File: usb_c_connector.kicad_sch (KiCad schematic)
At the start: 8 parts, among them J5 USB_C_Receptacle_USB2.0_16P, U4 USBLC6-2SC6

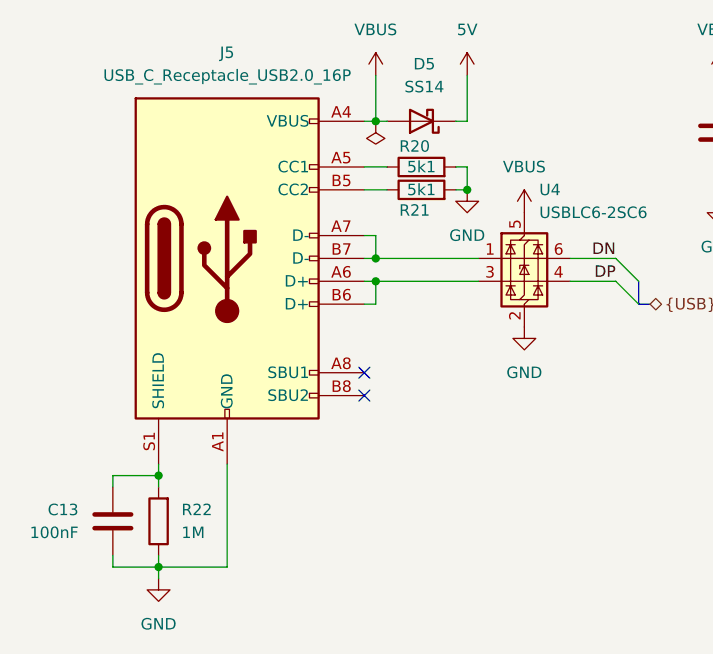
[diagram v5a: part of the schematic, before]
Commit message: Connect remaining tracks
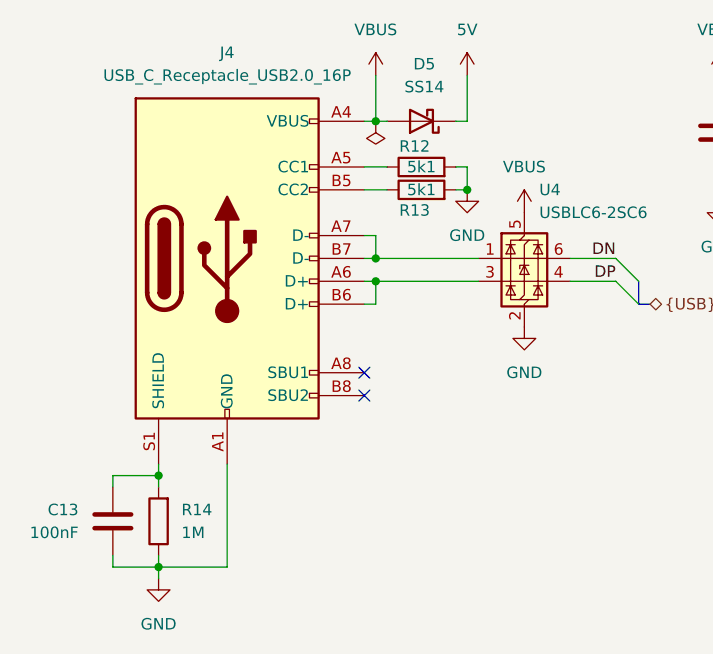
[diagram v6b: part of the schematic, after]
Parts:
- renumbered J5 to J4, R20 to R12, R21 to R13, R22 to R14
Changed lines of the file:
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@@
 		(on_board yes)
 		(dnp no)
-		(property "Reference" "R20"
+		(property "Reference" "R12"
 			(at 142.748 84.074 90)
 			(effects
@@
 			(project "Tumbler2_Redesign"
 				(path "/f3fd8d79-9d35-4c04-811e-2697a2740958/84b20f1f-6e00-4937-92e5-6e005c1bde3e"
-					(reference "R20")
+					(reference "R12")
 					(unit 1)
 				)
@@
 		(on_board yes)
 		(dnp no)
-		(property "Reference" "J5"
+		(property "Reference" "J4"
 			(at 121.92 73.66 0)
 			(effects
@@
 			(project "Tumbler2_Redesign"
 				(path "/f3fd8d79-9d35-4c04-811e-2697a2740958/84b20f1f-6e00-4937-92e5-6e005c1bde3e"
-					(reference "J5")
+					(reference "J4")
 					(unit 1)
 				)
@@
 		(on_board yes)
 		(dnp no)
-		(property "Reference" "R21"
+		(property "Reference" "R13"
 			(at 142.748 91.186 90)
 			(effects
@@
 			(project "Tumbler2_Redesign"
 				(path "/f3fd8d79-9d35-4c04-811e-2697a2740958/84b20f1f-6e00-4937-92e5-6e005c1bde3e"
-					(reference "R21")
+					(reference "R13")
 					(unit 1)
 				)
@@
 		(dnp no)
 		(fields_autoplaced yes)
-		(property "Reference" "R22"
+		(property "Reference" "R14"
 			(at 116.84 124.4599 0)
 			(effects
@@
 			(project "Tumbler2_Redesign"
 				(path "/f3fd8d79-9d35-4c04-811e-2697a2740958/84b20f1f-6e00-4937-92e5-6e005c1bde3e"
-					(reference "R22")
-					(unit 1)
-				)
+					(reference "R14")
+					(unit 1)
+				)

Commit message: cleanup schemati, replaced some caps from 0603 to 0805 around Linear Regulator
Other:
- company: (none) -> ${COMPANY}
- title: Tumbler 2 Redesign -> ${TITLE}
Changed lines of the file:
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@@
 	(paper "A4")
 	(title_block
-		(title "Tumbler 2 Redesign")
-		(rev "1.0")
+		(title "${TITLE}")
+		(rev "${REVISION}")
+		(company "${COMPANY}")
+		(comment 1 "${AUTHOR1}, ${AUTHOR2}, ${AUTHOR3} ")
+		(comment 2 "Stefan Kummer")
 	)
 	(junction
